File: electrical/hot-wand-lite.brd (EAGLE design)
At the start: 112 x 72 mm, 77 parts, among them IC1 12V R-78K12-2.0, IC2 AMS1117-5.0, Q1 NCHAN, Q2 SIRS5800DP-T1-GE3, Q3 DMTH64M2LPDWQ-13, Q4 2N7002K, Q5 G3404, U1 SEEED-XIAO-SAMD21, U2 1EDN8511BXUSA1, U3 LM74700QDBVTQ1, U4 AP53781

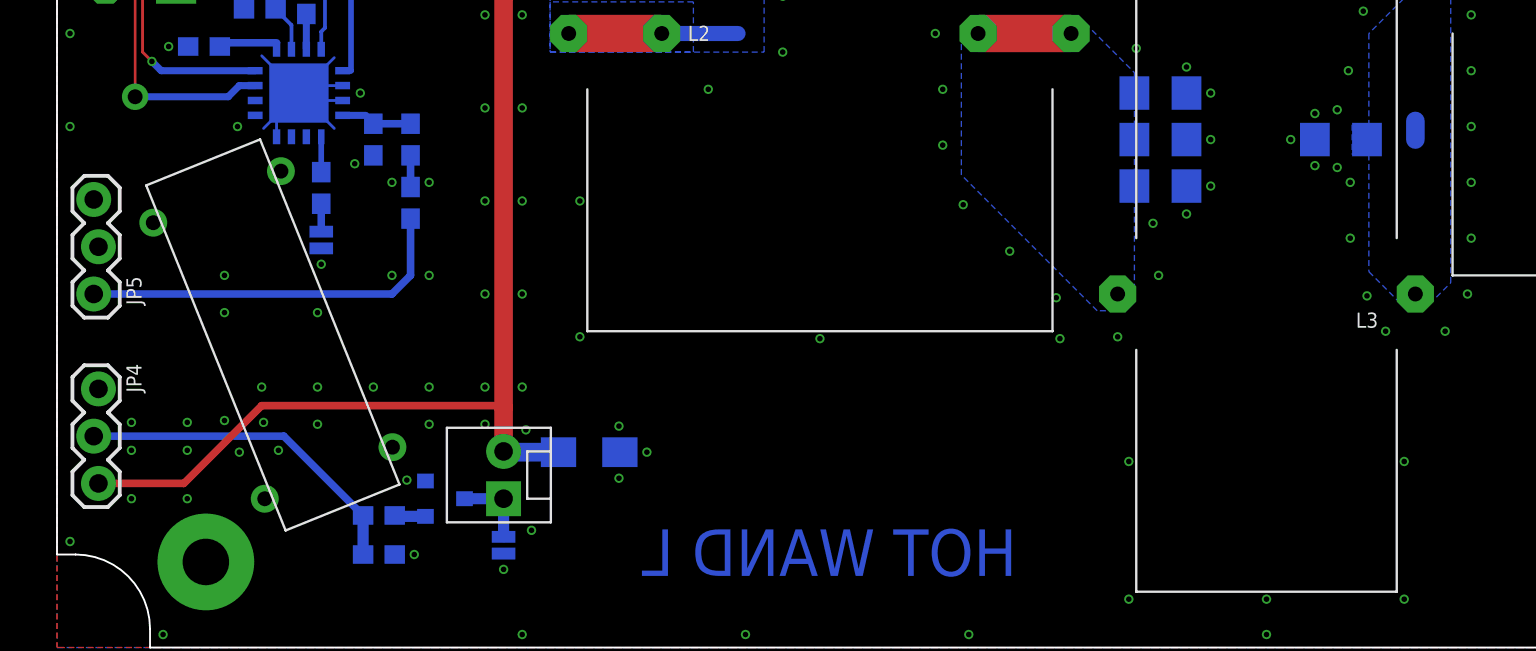
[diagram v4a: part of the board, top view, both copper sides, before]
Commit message: added a selector for ISEL
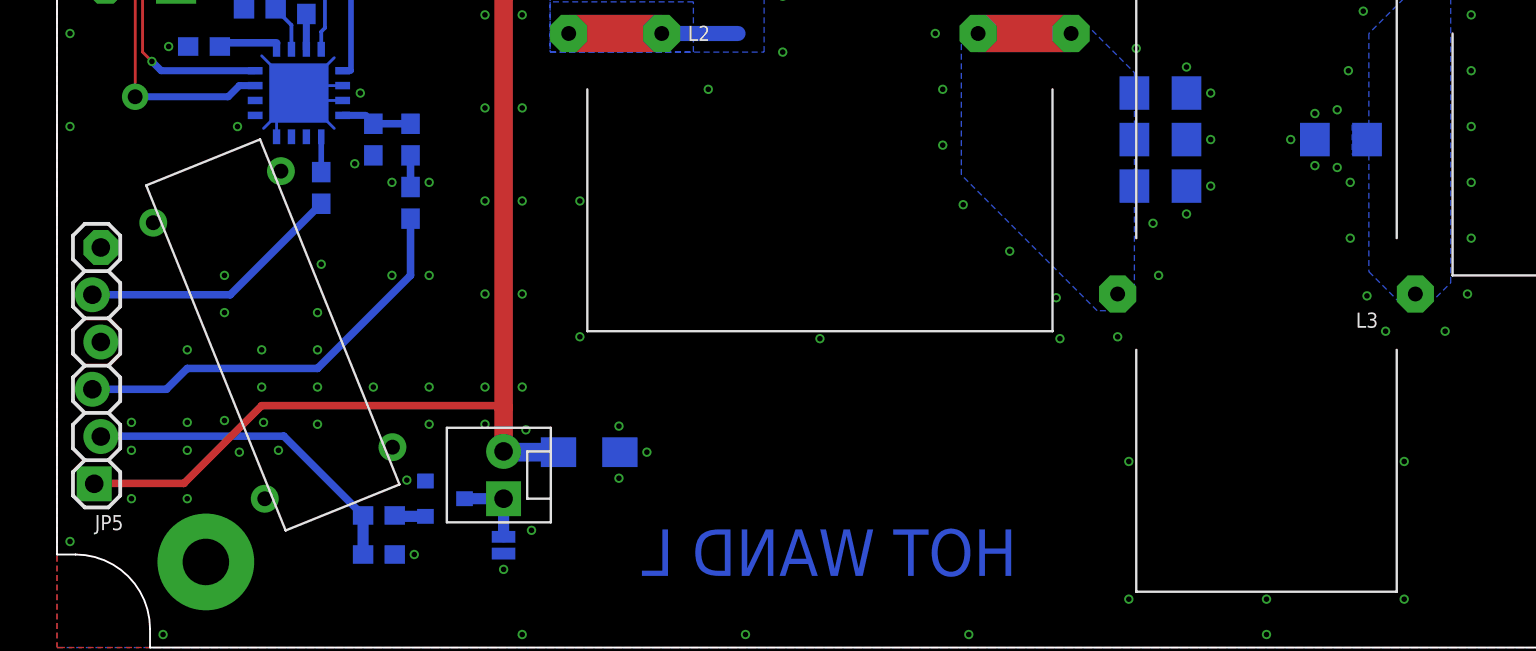
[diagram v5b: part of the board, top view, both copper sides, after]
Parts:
- removed JP4: (no value), hot-wand:1X03_LOCK
- removed SJ2: (no value), hot-wand:SJ_2S-NO
- JP5: device hot-wand:1X03_LOCK -> hot-wand:1X06_LOCK
- moved JP5 10.2 mm to (2.00, 8.80)
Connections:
- removed net N$55: R15.2, SJ2.1
- removed net N$9: JP5.1, R18.2
- removed net SWDIO: JP4.2, R7.1, R8.1
- new net FAN-CTRL: JP5.2, R7.1, R8.1
- new net USB-I-SEL: JP5.5, R15.2
- new net USB-V-SEL: JP5.3, R18.2
- net +12V: now also JP5.1; no longer JP4.3
- net GND: now also JP5.4, JP5.6; no longer JP4.1, JP5.2, JP5.3, SJ2.2
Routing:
- net USB-V-SEL: track 0.00 -> 22.7 mm
- net N$9: track 20.5 -> 0.00 mm
- net SWDIO: track 18.3 -> 0.00 mm
- net FAN-CTRL: track 0.00 -> 18.0 mm
- net USB-I-SEL: track 0.00 -> 14.3 mm
- net N$55: track 1.50 -> 0.00 mm
- net N$5: track 1.00 -> 0.00 mm
- net GND: vias 329 -> 332
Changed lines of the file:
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@@
 <attribute name="JLCPARTNUM" value="C23153" x="17" y="27.3" size="1.778" layer="28" rot="MR270" display="off"/>
-</element>
-<element name="SJ2" library="hot-wand" package="SJ_2S-NO" value="" x="14.2" y="21.9" smashed="yes" rot="MR270">
-<attribute name="NAME" x="12.83" y="22.208" size="0.8128" layer="26" font="fixed" rot="MR270"/>
-<attribute name="VALUE" x="15.851" y="22.808" size="0.4064" layer="28" rot="MR270"/>
-<attribute name="JLC-DNP" value="1" x="14.2" y="21.9" size="1.778" layer="28" rot="MR270" display="off"/>
 </element>
 <element name="SJ1" library="hot-wand" package="SJ_2S-NO" value="" x="24" y="5.5" smashed="yes" rot="MR90">
@@
 <attribute name="JLC-DNP" value="1" x="88" y="62" size="1.778" layer="27" rot="R270" display="off"/>
 </element>
-<element name="JP5" library="hot-wand" package="1X03_LOCK" value="" x="2.1" y="19" smashed="yes" rot="R90">
-<attribute name="NAME" x="3.7288" y="19.9462" size="0.8128" layer="25" font="fixed" ratio="10" rot="R270"/>
-<attribute name="VALUE" x="5.275" y="17.73" size="1.27" layer="27" rot="R90"/>
-<attribute name="JLC-DNP" value="1" x="2.1" y="19" size="1.778" layer="27" rot="R90" display="off"/>
-</element>
 <element name="R17" library="hot-wand" package="0603-RES" value="3K" x="19" y="27.3" smashed="yes" rot="MR270">
 <attribute name="NAME" x="19.862" y="27.911" size="0.8128" layer="26" font="fixed" rot="MR90"/>
@@
 <attribute name="JLC-DNP" value="1" x="110" y="54.4" size="1.778" layer="27" rot="R90" display="off"/>
 </element>
-<element name="JP4" library="hot-wand" package="1X03_LOCK" value="" x="2.1" y="13.9" smashed="yes" rot="R270">
-<attribute name="NAME" x="3.7288" y="15.2462" size="0.8128" layer="25" font="fixed" ratio="10" rot="R270"/>
-<attribute name="VALUE" x="-1.075" y="15.17" size="1.27" layer="27" rot="R270"/>
-<attribute name="JLC-DNP" value="1" x="2.1" y="13.9" size="1.778" layer="27" rot="R270" display="off"/>
-</element>
 <element name="R6" library="hot-wand" package="0603-RES" value="1K" x="108.4" y="44.3" smashed="yes" rot="MR270">
 <attribute name="JLCPARTNUM" value="C21190" x="108.4" y="44.3" size="1.778" layer="28" rot="MR270" display="off"/>
@@
 <attribute name="VALUE" x="20.857" y="22.784" size="0.8128" layer="28" font="vector" rot="MR90"/>
 <attribute name="JLCPARTNUM" value="C23242" x="19" y="23.9" size="1.778" layer="28" rot="MR270" display="off"/>
+</element>
+<element name="JP5" library="hot-wand" package="1X06_LOCK" value="" x="2" y="8.8" smashed="yes" rot="R90">
+<attribute name="NAME" x="3.57" y="7.122" size="0.8128" layer="25" font="fixed" rot="R180"/>
+<attribute name="VALUE" x="5.302" y="7.53" size="1.27" layer="27" font="vector" rot="R90"/>
 </element>
 </elements>
@@
 <contactref element="IC2" pad="1"/>
 <contactref element="U1" pad="13"/>
-<contactref element="SJ2" pad="2"/>
-<contactref element="JP5" pad="2"/>
 <contactref element="JP1" pad="2_1"/>
 <contactref element="JP1" pad="3_1"/>
@@
 <wire x1="111" y1="40.3" x2="111" y2="39.4" width="0.4064" layer="1"/>
 <contactref element="R16" pad="2"/>
-<contactref element="JP5" pad="3"/>
-<contactref element="JP4" pad="1"/>
 <via x="26.8" y="37.3" extent="1-16" drill="0.3" shape="octagon"/>
 <via x="38" y="37.3" extent="1-16" drill="0.3" shape="octagon"/>
@@
 <vertex x="48.5" y="67.7"/>
 </polygon>
+<contactref element="JP5" pad="4"/>
+<contactref element="JP5" pad="6"/>
+<via x="11" y="16" extent="1-16" drill="0.3" shape="octagon"/>
+<via x="14" y="16" extent="1-16" drill="0.3" shape="octagon"/>
+<via x="7" y="16" extent="1-16" drill="0.3" shape="octagon"/>
 </signal>
 <signal name="+24V">
@@
 <contactref element="C18" pad="2"/>
 <contactref element="IC2" pad="3"/>
-<contactref element="JP4" pad="3"/>
 <wire x1="24" y1="10.54" x2="24" y2="12.9" width="1" layer="1"/>
 <wire x1="24" y1="12.9" x2="24" y2="35" width="1" layer="1"/>
@@
 <wire x1="54.55" y1="64.6" x2="54.55" y2="61.6" width="0.6" layer="16"/>
 <wire x1="54.55" y1="61.6" x2="54" y2="61.6" width="0.6" layer="16"/>
-<wire x1="2.227" y1="8.82" x2="6.82" y2="8.82" width="0.4064" layer="1"/>
 <wire x1="6.82" y1="8.82" x2="11" y2="13" width="0.4064" layer="1"/>
 <wire x1="11" y1="13" x2="24" y2="13" width="0.4064" layer="1"/>
@@
 <wire x1="26.95" y1="10.5" x2="24" y2="10.5" width="1" layer="16"/>
 <wire x1="24" y1="10.5" x2="24" y2="10.54" width="1" layer="16"/>
+<contactref element="JP5" pad="1"/>
+<wire x1="6.82" y1="8.82" x2="2.02" y2="8.82" width="0.4064" layer="1"/>
+<wire x1="2.02" y1="8.82" x2="2" y2="8.8" width="0.4064" layer="1"/>
 </signal>
 <signal name="MCU-RF">
@@
 <wire x1="14.2" y1="27.45" x2="14.2" y2="25.55" width="0.3048" layer="16"/>
 </signal>
-<signal name="N$55">
-<contactref element="R15" pad="2"/>
-<contactref element="SJ2" pad="1"/>
-<wire x1="14.2" y1="23.85" x2="14.2" y2="22.35" width="0.4064" layer="16"/>
-</signal>
 <signal name="N$57">
 <contactref element="R13" pad="2"/>
@@
 <contactref element="L4" pad="1"/>
 <contactref element="C9" pad="2"/>
-<wire x1="73" y1="27.3" x2="73" y2="28.3" width="1" layer="16"/>
 <polygon width="0.2032" layer="16" spacing="0.2032" isolate="0.6096" thermals="no" rank="3">
 <vertex x="72.1" y="18.6"/>
@@
 </polygon>
 </signal>
-<signal name="SWDIO">
+<signal name="FAN-CTRL">
 <contactref element="R7" pad="1"/>
 <contactref element="R8" pad="1"/>
-<contactref element="JP4" pad="2"/>
 <wire x1="16.45" y1="7.1" x2="12.19" y2="11.36" width="0.4064" layer="16"/>
-<wire x1="12.19" y1="11.36" x2="1.973" y2="11.36" width="0.4064" layer="16"/>
 <wire x1="16.45" y1="5" x2="16.45" y2="7.1" width="0.6" layer="16"/>
+<contactref element="JP5" pad="2"/>
+<wire x1="12.19" y1="11.36" x2="2.374" y2="11.36" width="0.4064" layer="16"/>
+<wire x1="2.374" y1="11.36" x2="2.354" y2="11.34" width="0.4064" layer="16"/>
 </signal>
 <signal name="5V">
@@
 <contactref element="U1" pad="12"/>
 </signal>
-<signal name="N$9">
-<contactref element="JP5" pad="1"/>
-<wire x1="19" y1="20" x2="18" y2="19" width="0.4064" layer="16"/>
-<wire x1="18" y1="19" x2="1.973" y2="19" width="0.4064" layer="16"/>
+<signal name="USB-V-SEL">
 <contactref element="R18" pad="2"/>
 <wire x1="19" y1="23.05" x2="19" y2="20" width="0.4064" layer="16"/>
+<contactref element="JP5" pad="3"/>
+<wire x1="19" y1="20" x2="14" y2="15" width="0.4064" layer="16"/>
+<wire x1="14" y1="15" x2="7" y2="15" width="0.4064" layer="16"/>
+<wire x1="7" y1="15" x2="5.88" y2="13.88" width="0.4064" layer="16"/>
+<wire x1="5.88" y1="13.88" x2="1.9" y2="13.88" width="0.4064" layer="16"/>
 </signal>
 <signal name="SEL3">
@@
 <wire x1="19" y1="26.45" x2="19" y2="24.75" width="0.4064" layer="16"/>
 </signal>
+<signal name="USB-I-SEL">
+<contactref element="JP5" pad="5"/>
+<contactref element="R15" pad="2"/>
+<wire x1="14.2" y1="23.85" x2="9.31" y2="18.96" width="0.4064" layer="16"/>
+<wire x1="9.31" y1="18.96" x2="1.9" y2="18.96" width="0.4064" layer="16"/>
+</signal>
 </signals>

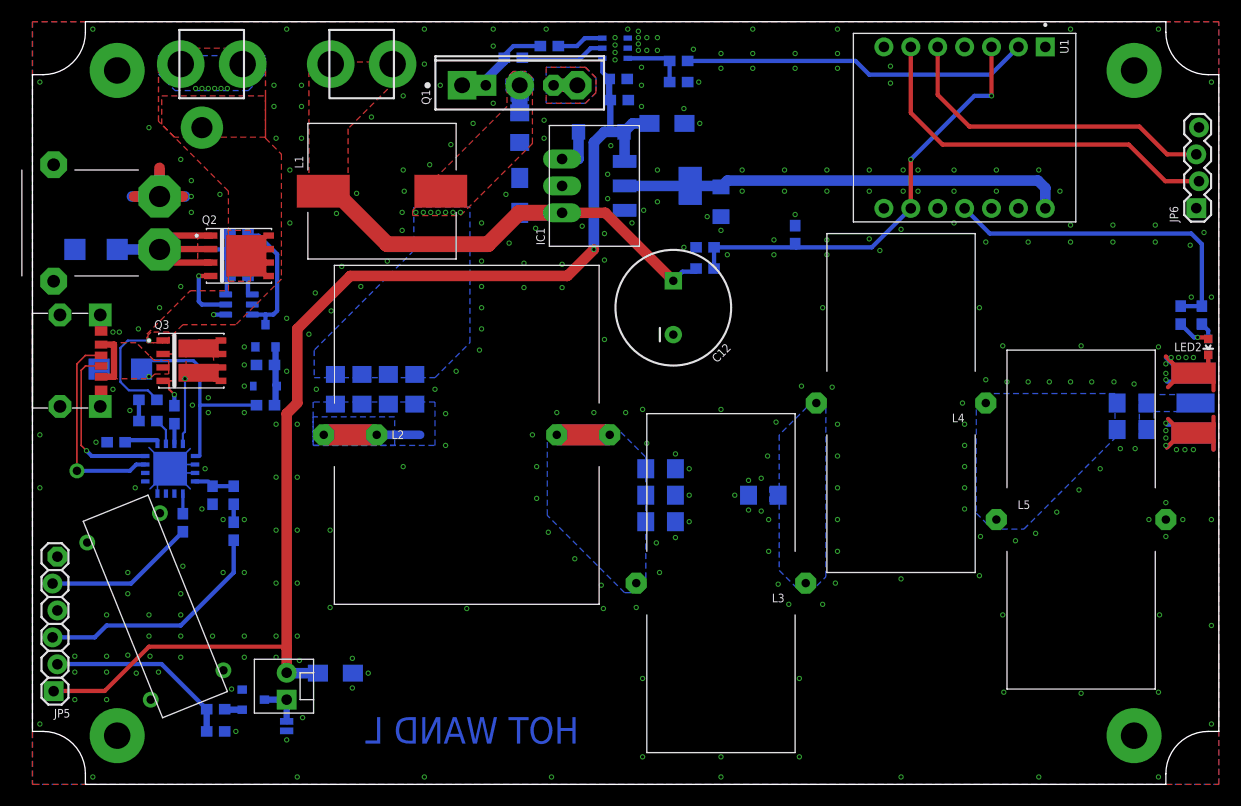
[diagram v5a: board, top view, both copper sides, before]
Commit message: lite, major design change, now 15V or 20V, 3A or 5A, no mosfet for fan
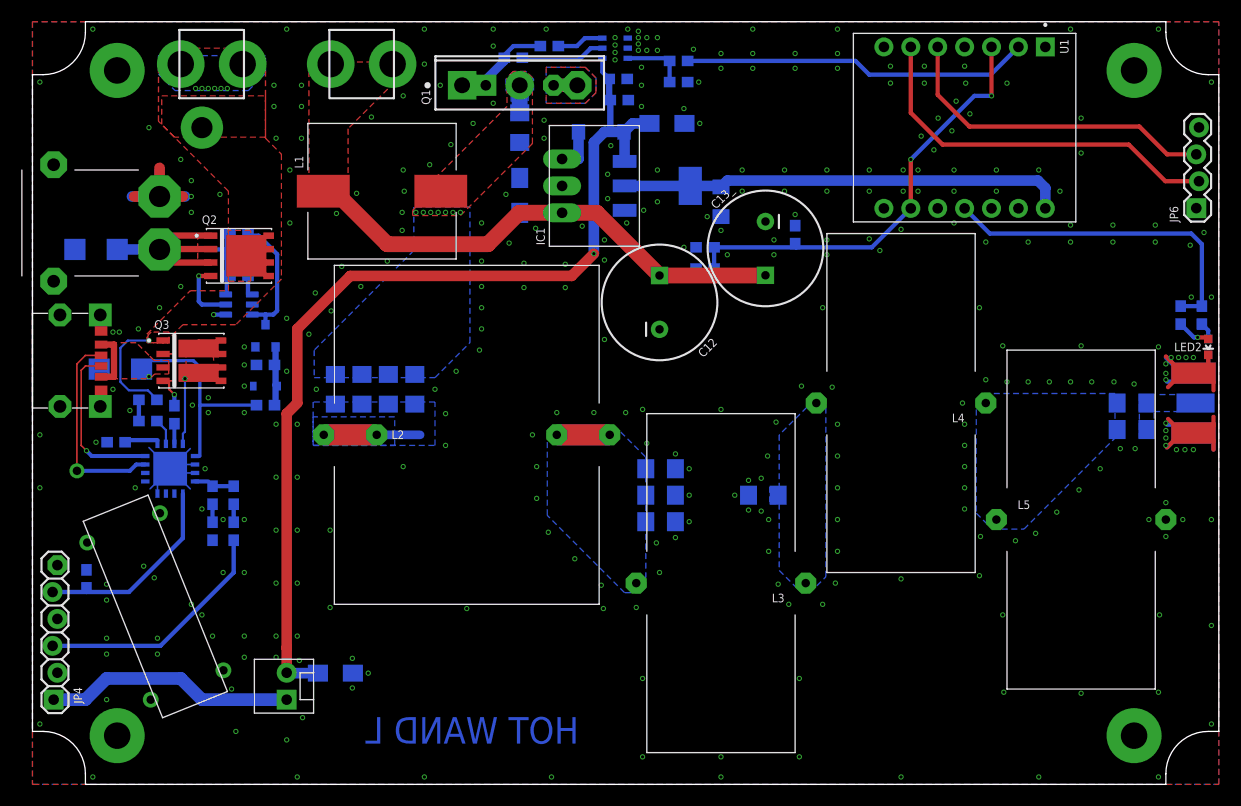
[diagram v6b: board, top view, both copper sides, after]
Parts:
- removed JP5: (no value), hot-wand:1X06_LOCK
- removed Q5: G3404, hot-wand:SOT23-3
- removed R15: DNP, hot-wand:0603-RES
- removed R7: 4K7, hot-wand:0603-RES
- removed SJ1: (no value), hot-wand:SJ_2S-NO
- added C13_: 470u, hot-wand:CPOL-RADIAL-1000UF-25V
- added JP4: (no value), hot-wand:1X06_LOCK
- added R17_: 1K, hot-wand:0603-RES
- R16: value 39K -> 51K
- R17: value 3K -> 100K
- R18: value 75K -> 56K
- R8: value 470Ω -> 26K
- moved R8 17.3 mm to (5.10, 19.4), turned to 90 degrees
- moved C12 1.39 mm to (59.2, 45.5)
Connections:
- removed net N$52: FAN1.1, Q5.3, SJ1.2
- removed net N$53: Q5.1, R8.2
- removed net N$54: R15.1, U4.5
- new net N$9: R16.2, R17_.1
- net +12V: no longer JP5.1
- net +24V: now also C13_.1
- net FAN-CTRL: now also FAN1.1, JP4.1; no longer JP5.2, R7.1, R8.1
- net GND: now also C13_.2, JP4.2, JP4.4, JP4.6, R17_.2, R8.2; no longer JP5.4, JP5.6, Q5.2, R16.2, R7.2, SJ1.1
- net USB-I-SEL: now also JP4.5, R8.1, U4.5; no longer JP5.5, R15.2
- net USB-V-SEL: now also JP4.3; no longer JP5.3
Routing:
- net +12V: track 117.6 -> 94.1 mm
- net FAN-CTRL: track 18.0 -> 23.7 mm
- net +24V: track 44.6 -> 50.0 mm
- net USB-I-SEL: track 14.3 -> 19.0 mm
- net N$52: track 4.15 -> 0.00 mm
- net N$54: track 1.90 -> 0.00 mm
- net N$53: track 1.70 -> 0.00 mm
- net N$9: track 0.00 -> 1.70 mm
- net GND: vias 332 -> 336
